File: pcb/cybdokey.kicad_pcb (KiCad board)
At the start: 2 copper layers, 12 x 26 mm, 39 parts, among them J1 USB_A, U1 RP2354_60QFN, U2 MCP1700x-300xxTT, U3 USBLC6-2P6, Y1 ABM8-272-T3

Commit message: more routing
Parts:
- added TP2: run, TestPoint:TestPoint_Pad_1.0x1.0mm, F.Cu at (211.5, 76.7)
- added TP3: 3V3, TestPoint:TestPoint_Pad_1.0x1.0mm, F.Cu at (212.3, 72.3)
- added TP4: GND, TestPoint:TestPoint_Pad_1.0x1.0mm, F.Cu at (204.9, 77.1)
- moved JP1 156.2 mm to (197.4, 68.8), turned to 180 degrees
- moved C18 145.8 mm to (213.9, 73.4), turned to 90 degrees
- moved Y1 145.3 mm to (216.4, 72.7), turned to 90 degrees
- moved C10 142.8 mm to (213.9, 71.2), turned to -90 degrees
- moved C11 141.5 mm to (211.2, 63.3), turned to -90 degrees
- moved C16 141.1 mm to (219.3, 70.1)
- moved C19 140.8 mm to (218.7, 73.9), turned to -90 degrees
- moved R4 138.4 mm to (207.7, 62.2), turned to 180 degrees
- moved C17 137.0 mm to (220.6, 64.5), turned to 90 degrees
- moved L1 136.2 mm to (218.2, 59.1)
- moved R1 135.6 mm to (212.1, 59.9), turned to 90 degrees
- moved R2 133.9 mm to (213.1, 59.9), turned to 90 degrees
- moved R5 133.8 mm to (211.0, 59.8), turned to 90 degrees
- moved C15 133.6 mm to (223.8, 59.6)
- moved C12 133.3 mm to (220.6, 66.8), turned to -90 degrees
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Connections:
- U1 pad 26: /RUN -> Net-(U1-RUN)
- U3 pad 1: /USB_D+ -> /USB_D-
- U3 pad 3: /USB_D- -> /USB_D+
- U3 pad 4: /PROT_USB_D- -> /PROT_USB_D+
- U3 pad 6: /PROT_USB_D+ -> /PROT_USB_D-
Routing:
- net +3V3: track 0.00 -> 32.4 mm, vias 0 -> 7
- net +1V1: track 0.00 -> 27.8 mm
- net GND: track 0.66 -> 20.0 mm, vias 2 -> 10
- net Net-(U1-USB_DP): track 0.00 -> 5.66 mm
- net /XIN: track 0.00 -> 5.00 mm
- net Net-(U1-USB_DM): track 0.00 -> 4.93 mm
- net /XOUT: track 0.00 -> 4.57 mm
- net Net-(U1-VREG_LX): track 0.00 -> 3.84 mm
- net /QSPI_SS: track 0.00 -> 3.42 mm
- net Net-(C19-Pad1): track 0.00 -> 2.81 mm
- net /USB_D-: track 14.3 -> 11.7 mm
- net /PROT_USB_D-: track 0.00 -> 1.27 mm
- net /PROT_USB_D+: track 0.00 -> 1.25 mm
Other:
- board size 12 x 26 mm -> 12 x 36 mm

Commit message: routing done... for now
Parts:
- removed C13, C14: 100nF, Capacitor_SMD:C_0402_1005Metric_Pad0.74x0.62mm_HandSolder
- removed JP2: SolderJumper_2_Open, Jumper:SolderJumper-2_P1.3mm_Open_TrianglePad1.0x1.5mm
- removed R8: 10kR, Resistor_SMD:R_0402_1005Metric_Pad0.72x0.64mm_HandSolder
- removed R9: 1kR, Resistor_SMD:R_0402_1005Metric_Pad0.72x0.64mm_HandSolder
- D2: moved to B.Cu
- moved C8 30.4 mm to (211.2, 69.1), turned to -90 degrees
- moved C9 22.9 mm to (221.0, 71.0), turned to -90 degrees
- moved D2 19.7 mm to (216.2, 79.2), turned to 180 degrees
- moved TP3 16.1 mm to (220.9, 58.6)
- moved TP4 15.6 mm to (220.4, 75.3)
- moved JP1 15.2 mm to (211.7, 74.0), turned to 90 degrees
- moved R4 14.5 mm to (211.8, 76.2)
- moved C15 14.5 mm to (211.2, 66.9), turned to -90 degrees
- moved C5 13.4 mm to (220.0, 60.9), turned to 90 degrees
- moved R7 10.6 mm to (210.8, 80.9)
- moved R3 10.3 mm to (220.9, 60.9), turned to -90 degrees
- moved TP2 9.59 mm to (220.4, 73.2)
- moved C1 6.12 mm to (218.7, 58.1)
- moved C2 5.22 mm to (215.0, 60.2), turned to -90 degrees
- moved C3 3.07 mm to (218.2, 61.8), turned to 0 degrees
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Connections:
- U1 pad 15: unconnected-(U1-GPIO11-Pad15) -> /TOUCH_BTN
- U1 pad 17: /TOUCH_BTN -> unconnected-(U1-GPIO13-Pad17)
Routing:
- net +3V3: track 32.4 -> 89.2 mm, vias 7 -> 10
- net GND: track 20.0 -> 37.6 mm, vias 10 -> 32
- net /TOUCH_BTN: track 0.00 -> 11.8 mm, vias 0 -> 2
- net /QSPI_SS: track 3.42 -> 14.0 mm, vias 0 -> 2
- net /LED: track 0.00 -> 8.29 mm, vias 0 -> 1
- net Net-(U1-RUN): track 0.00 -> 5.99 mm, vias 0 -> 2
- net Net-(R7-Pad1): track 0.00 -> 4.13 mm, vias 0 -> 1
- net Net-(U1-VREG_AVDD): track 0.00 -> 3.74 mm
- net VSYS: track 1.57 -> 3.63 mm
- net +1V1: track 27.8 -> 29.7 mm, vias 0 -> 1
- net Net-(JP1-A): track 0.00 -> 1.69 mm
- net /USB_D-: track 11.7 -> 13.1 mm
- net /USB_D+: track 10.9 -> 12.3 mm
- net Net-(U1-VREG_LX): track 3.84 -> 5.06 mm
- net VBUS: track 21.5 -> 22.4 mm
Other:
- board size 12 x 36 mm -> 12 x 50 mm

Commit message: cleaned up routing
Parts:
- D2: footprint LED_SMD:LED_WS2812B_PLCC4_5.0x5.0mm_P3.2mm -> imports:SK6812MINI-E_fixed
- moved TP1 5.17 mm to (216.1, 81.0)
- moved R7 2.34 mm to (210.9, 78.6)
- moved D2 1.86 mm to (216.1, 81.1)
- moved R3 0.10 mm to (221.1, 60.9)
- moved C5 0.10 mm to (220.1, 60.9)
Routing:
- net GND: track 37.6 -> 49.0 mm, vias 32 -> 31
- net +3V3: track 89.2 -> 85.5 mm
- net /LED: track 8.29 -> 11.9 mm, vias 1 -> 2
- net /TOUCH_BTN: track 11.8 -> 9.45 mm
- net Net-(R7-Pad1): track 4.13 -> 4.84 mm
- net VBUS: track 22.4 -> 21.7 mm
- net +1V1: vias 1 -> 0

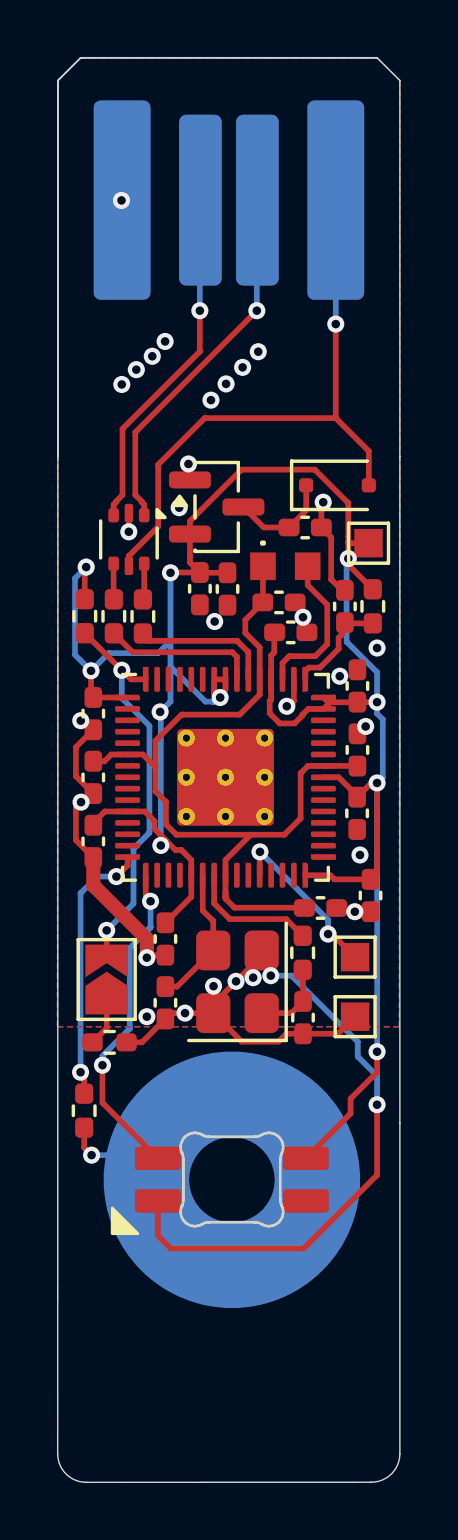
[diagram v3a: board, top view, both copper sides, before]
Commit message: cleaned up routing the second
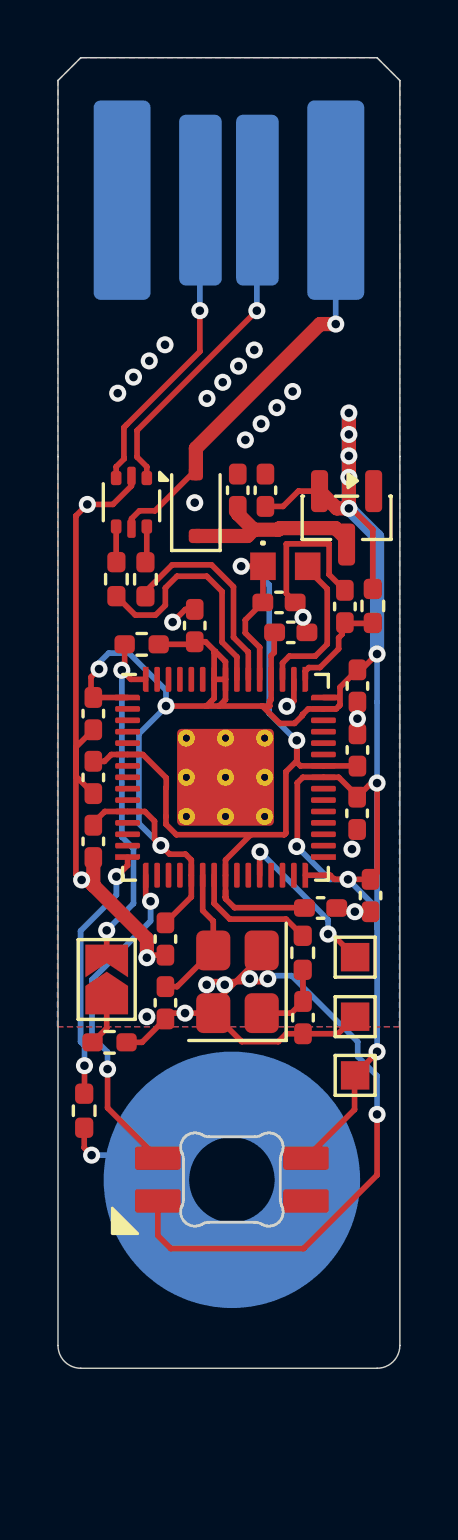
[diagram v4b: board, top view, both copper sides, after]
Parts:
- moved TP3 18.7 mm to (220.4, 77.3)
- moved D1 5.02 mm to (214.8, 57.3), turned to 90 degrees
- moved U2 4.58 mm to (220.1, 57.8), turned to -90 degrees
- moved C2 4.15 mm to (217.3, 56.8), turned to 90 degrees
- moved C1 2.70 mm to (216.3, 56.8), turned to 90 degrees
- moved R5 2.23 mm to (212.9, 62.2), turned to 0 degrees
- moved C6 1.72 mm to (214.8, 61.5), turned to 90 degrees
- moved R1 1.31 mm to (212.1, 59.9)
- moved R2 1.31 mm to (213.1, 59.9)
- moved U3 1.31 mm to (212.6, 57.2)
- turned C7 to -90 degrees
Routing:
- net GND: track 49.0 -> 68.0 mm, vias 31 -> 29
- net +3V3: track 85.5 -> 92.7 mm, vias 10 -> 13
- net VBUS: track 21.7 -> 15.2 mm
- net +1V1: track 29.7 -> 33.7 mm, vias 0 -> 2
- net VSYS: track 3.63 -> 6.80 mm
- net Net-(U1-USB_DP): track 5.45 -> 8.44 mm
- net Net-(U1-USB_DM): track 4.95 -> 7.49 mm
- net /QSPI_SS: track 14.0 -> 12.6 mm
- net /USB_D+: track 12.3 -> 11.0 mm
- net /USB_D-: track 13.1 -> 11.7 mm
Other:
- board size 12 x 50 mm -> 12 x 32 mm

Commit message: changed LED, moving back to windows
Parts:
- removed D2: WS2812B, imports:SK6812MINI-E_fixed
- added D3: LED_RKBG, LED_SMD:LED_Kingbright_AAA3528ESGCT, F.Cu at (216.1, 81.0)
- moved C18 0.45 mm to (213.9, 75.2)
- moved C10 0.45 mm to (213.9, 73.0)
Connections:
- U1 pad 16: /LED -> /LED_G
- U1 pad 18: unconnected-(U1-GPIO14-Pad18) -> /LED_R
- U1 pad 4: unconnected-(U1-GPIO2-Pad4) -> /LED_B
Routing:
- net /LED_G: track 0.00 -> 13.1 mm, vias 0 -> 2
- net /LED: track 12.0 -> 0.00 mm, vias 2 -> 0
- net /LED_R: track 0.00 -> 11.6 mm, vias 0 -> 2
- net GND: track 68.0 -> 57.3 mm, vias 29 -> 28
- net /LED_B: track 0.00 -> 6.29 mm, vias 0 -> 1
- net +3V3: track 92.7 -> 90.5 mm
- net /QSPI_SS: track 12.6 -> 13.1 mm

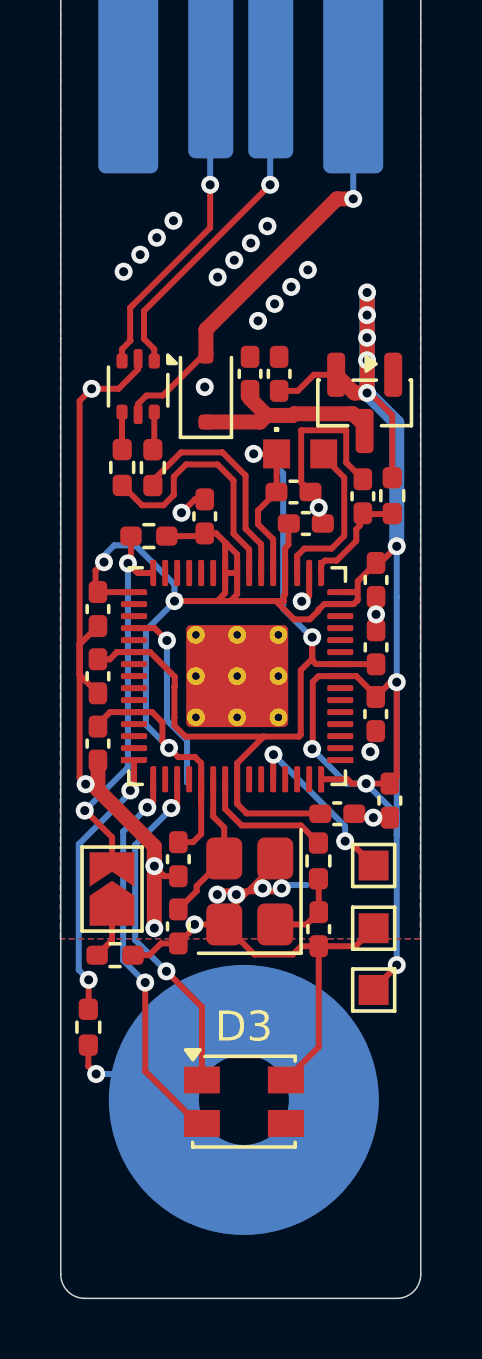
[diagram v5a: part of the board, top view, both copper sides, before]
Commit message: add new touch button footprint and add some branding
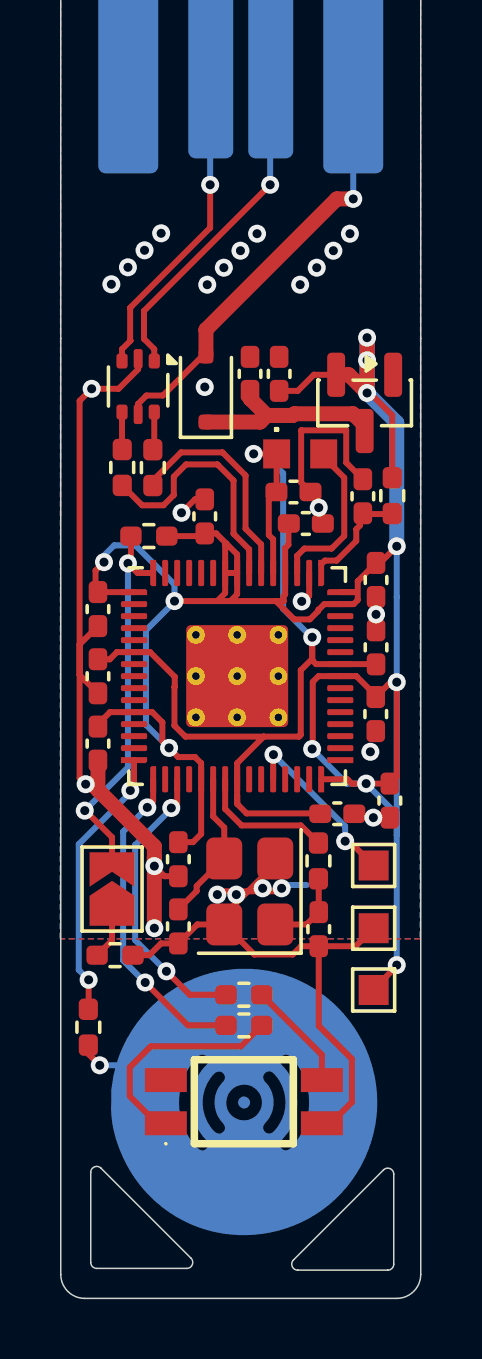
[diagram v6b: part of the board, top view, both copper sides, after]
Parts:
- added R8: 220R, Resistor_SMD:R_0402_1005Metric_Pad0.72x0.64mm_HandSolder, F.Cu at (216.1, 77.5)
- added R9: 220R, Resistor_SMD:R_0402_1005Metric_Pad0.72x0.64mm_HandSolder, F.Cu at (216.1, 78.5)
- D3: footprint LED_SMD:LED_Kingbright_AAA3528ESGCT -> imports:LED-SMD_4P-L3.2-W2.8_XZMDKCBDDG45S-9
- turned D3 to 180 degrees
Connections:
- D3 pad 1: /LED_R -> Net-(D3-RA)
- D3 pad 3: /LED_B -> Net-(D3-BA)
- D3 pad 4: /LED_G -> unconnected-(D3-GA-Pad4)
- U1 pad 4: /LED_B -> unconnected-(U1-GPIO2-Pad4)
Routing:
- net /LED_G: track 13.1 -> 0.00 mm, vias 2 -> 0
- net /LED_R: track 11.6 -> 20.6 mm, vias 2 -> 4
- net Net-(D3-RA): track 0.00 -> 7.52 mm
- net /LED_B: track 6.29 -> 0.00 mm, vias 1 -> 0
- net +3V3: track 90.5 -> 85.6 mm, vias 13 -> 11
- net Net-(D3-BA): track 0.00 -> 3.67 mm
- net +1V1: track 33.7 -> 33.2 mm
- net GND: track 57.3 -> 57.7 mm, vias 28 -> 27
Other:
- outline, holes or cut-outs redrawn

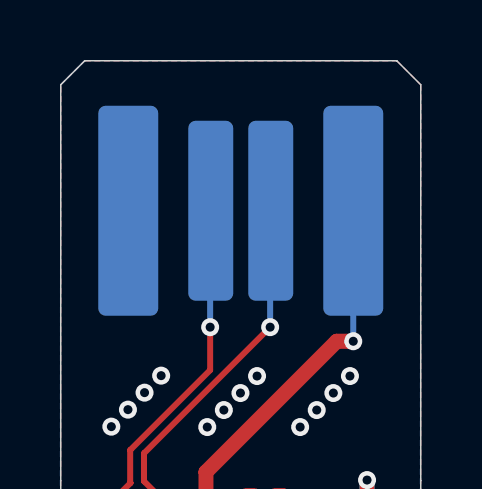
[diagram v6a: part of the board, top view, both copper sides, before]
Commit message: add cybdokey branding
i forgor
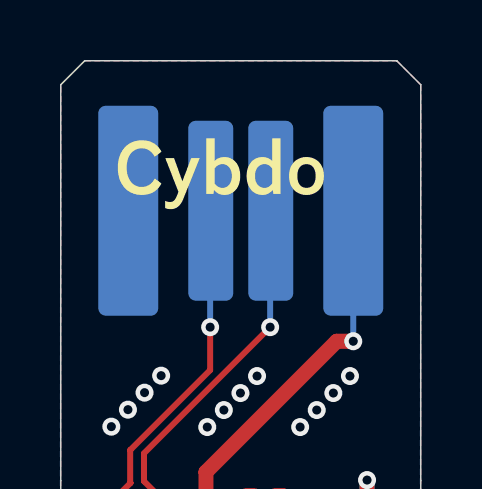
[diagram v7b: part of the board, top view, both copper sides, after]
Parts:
- added REF**: cybdokey, imports:cybdokey, F.Cu at (213.1, 42.6)

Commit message: polishing, started with some renders
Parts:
- added REF**: cybdokey, imports:cybdokey, B.Cu at (218.9, 55.5)
- moved C4 1.60 mm to (216.9, 59.4), turned to 180 degrees
- moved L1 1.12 mm to (218.8, 60.2), turned to -90 degrees
- moved C3 0.98 mm to (217.5, 61.0), turned to 90 degrees
- moved C5 0.22 mm to (220.0, 61.1)
- moved R3 0.22 mm to (221.0, 61.1)
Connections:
- U1 pad 16: /LED_G -> /LED_B
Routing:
- net GND: track 57.7 -> 70.8 mm, vias 27 -> 28
- net /LED_B: track 0.00 -> 11.6 mm, vias 0 -> 2
- net /LED_R: track 20.6 -> 10.8 mm, vias 4 -> 2
- net +1V1: track 33.2 -> 29.7 mm, vias 2 -> 0
- net Net-(U1-VREG_LX): track 5.33 -> 2.83 mm
- net +3V3: track 85.6 -> 87.3 mm, vias 11 -> 13
- net VBUS: track 15.1 -> 16.7 mm, vias 1 -> 3
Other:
- board text added: ". L1"
